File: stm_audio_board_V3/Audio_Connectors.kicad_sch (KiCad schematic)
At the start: 8 parts, among them J12 AudioJack_Loop2_Send, J13 AudioJack_Loop1_Send, J14 AudioJack_OUTPUT_Main, J15 AudioJack_Loop3_Return, J16 AudioJack_Loop2_Return, J7 AudioJack_Loop3_Send, J8 AudioJack_Loop1_Return, J9 AudioJack_INPUT_Main

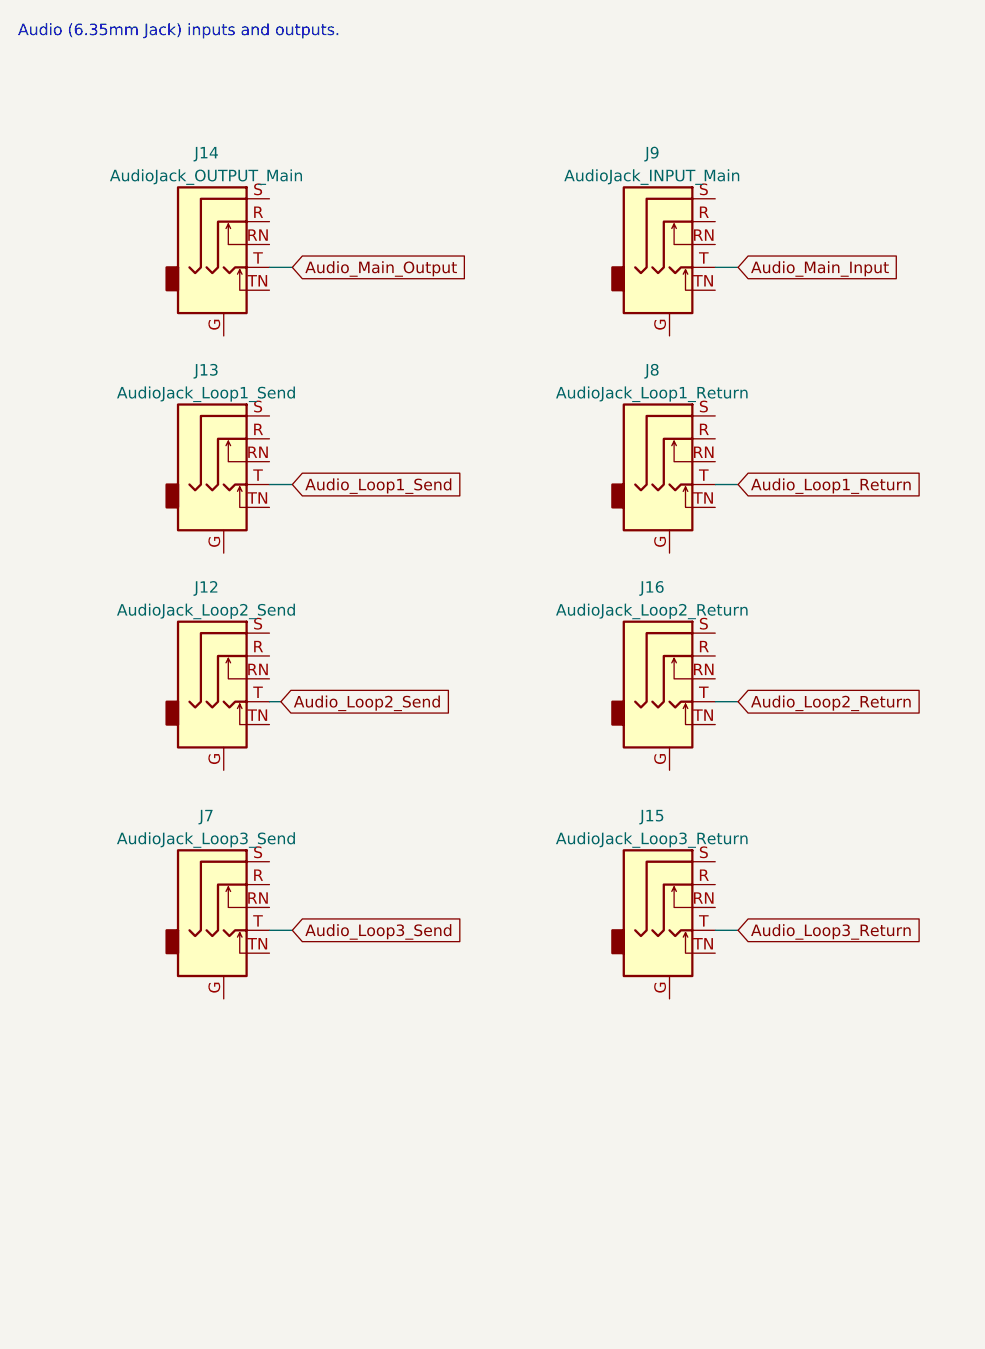
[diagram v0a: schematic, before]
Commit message: Reworked outline for enclosure
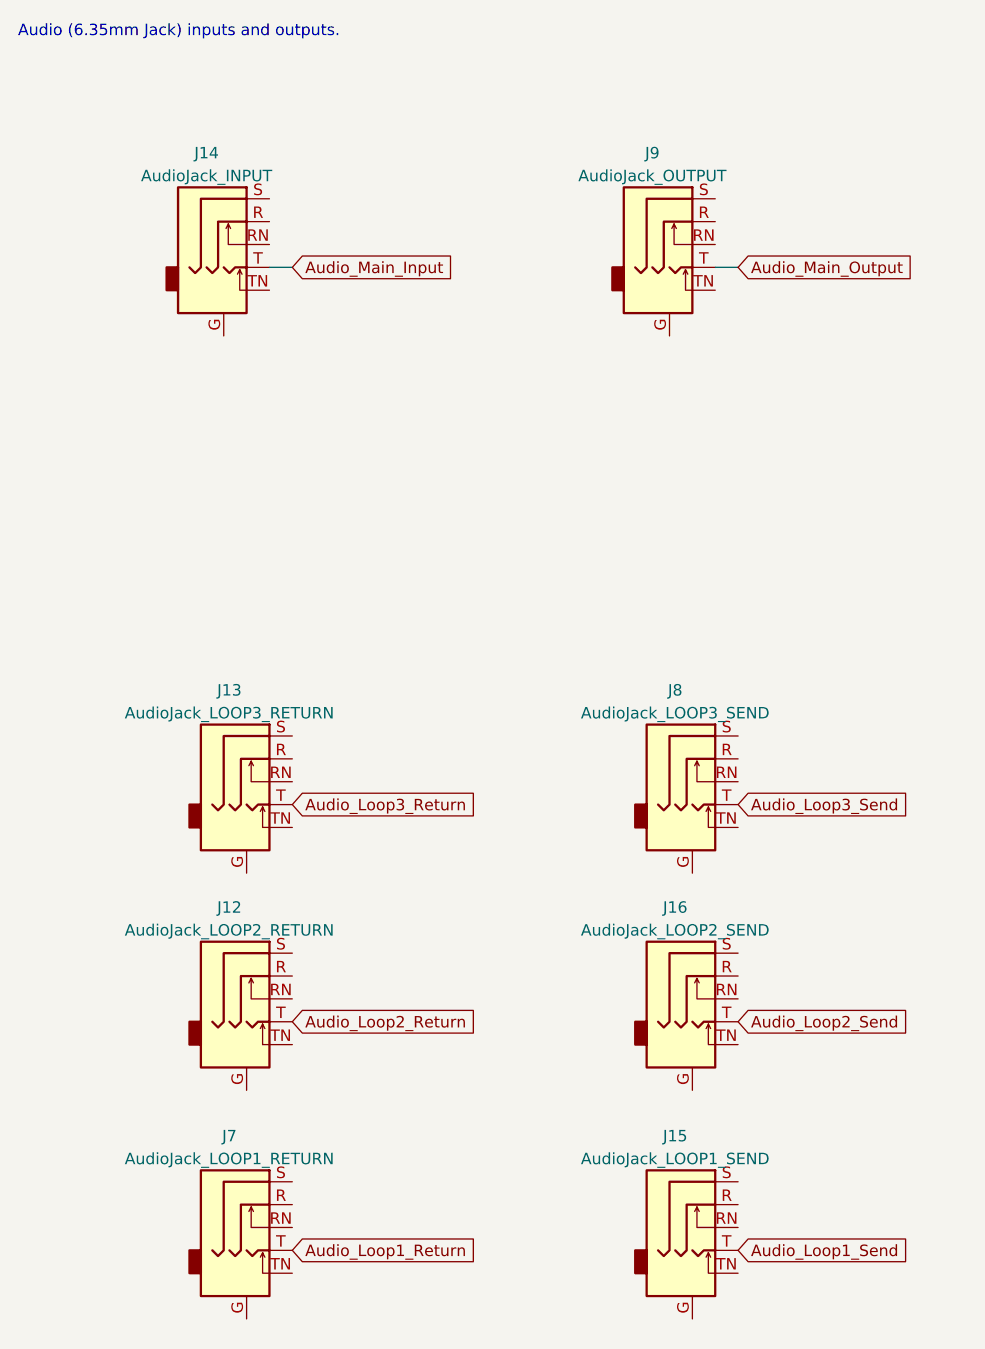
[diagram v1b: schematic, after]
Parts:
- J12: value AudioJack_Loop2_Send -> AudioJack_LOOP2_RETURN
- J13: value AudioJack_Loop1_Send -> AudioJack_LOOP3_RETURN
- J14: value AudioJack_OUTPUT_Main -> AudioJack_INPUT
- J15: value AudioJack_Loop3_Return -> AudioJack_LOOP1_SEND
- J16: value AudioJack_Loop2_Return -> AudioJack_LOOP2_SEND
- J7: value AudioJack_Loop3_Send -> AudioJack_LOOP1_RETURN
- J8: value AudioJack_Loop1_Return -> AudioJack_LOOP3_SEND
- J9: value AudioJack_INPUT_Main -> AudioJack_OUTPUT
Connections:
- net Audio_Loop1_Return: now also J7.T; no longer J8.T
- net Audio_Loop1_Send: now also J15.T; no longer J13.T
- net Audio_Loop2_Return: now also J12.T; no longer J16.T
- net Audio_Loop2_Send: now also J16.T; no longer J12.T
- net Audio_Loop3_Return: now also J13.T; no longer J15.T
- net Audio_Loop3_Send: now also J8.T; no longer J7.T
- net Audio_Main_Input: now also J14.T; no longer J9.T
- net Audio_Main_Output: now also J9.T; no longer J14.T
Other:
- moved on the sheet: J12, J13, J15, J16, J7, J8

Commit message: PCB design is finished
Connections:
- net GND: now reaches J14.TN
- net GND: now also J12.TN, J13.TN, J7.TN
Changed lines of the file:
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@@
+    )
+  )
+  (symbol (lib_id "power:GND") (at 45.72 45.72 0) (unit 1)
+    (in_bom yes) (on_board yes) (dnp no) (fields_autoplaced)
+    (property "Reference" "#PWR02" (at 45.72 52.07 0)
+      (effects (font (size 1.27 1.27)) hide)
+    )
+    (property "Value" "GND" (at 45.72 50.8 0)
+      (effects (font (size 1.27 1.27)))
+    )
+    (property "Footprint" "" (at 45.72 45.72 0)
+      (effects (font (size 1.27 1.27)) hide)
+    )
+    (property "Datasheet" "" (at 45.72 45.72 0)
+      (effects (font (size 1.27 1.27)) hide)
+    )
+    (pin "1")
+    (instances
+      (project "stm_audio_board_V3"
+        (path "/6997cf63-2615-4e49-9471-e7da1b6bae71"
+          (reference "#PWR02") (unit 1)
+        )
+        (path "/6997cf63-2615-4e49-9471-e7da1b6bae71/2eb2ee8f-ab98-4666-97f0-bfacb073bc88"
+          (reference "#PWR01") (unit 1)
+        )
+        (path "/6997cf63-2615-4e49-9471-e7da1b6bae71/f20dc640-ad21-4977-8df1-611625087c69"
+          (reference "#PWR013") (unit 1)
+        )
+        (path "/6997cf63-2615-4e49-9471-e7da1b6bae71/bf8ef258-4ec0-4b8f-b717-0a82eb791e29"
+          (reference "#PWR0249") (unit 1)
+        )
+      )
+    )
+  )
+  (symbol (lib_id "power:GND") (at 48.26 154.94 0) (unit 1)
+    (in_bom yes) (on_board yes) (dnp no) (fields_autoplaced)
+    (property "Reference" "#PWR02" (at 48.26 161.29 0)
+      (effects (font (size 1.27 1.27)) hide)
+    )
+    (property "Value" "GND" (at 48.26 160.02 0)
+      (effects (font (size 1.27 1.27)))
+    )
+    (property "Footprint" "" (at 48.26 154.94 0)
+      (effects (font (size 1.27 1.27)) hide)
+    )
+    (property "Datasheet" "" (at 48.26 154.94 0)
+      (effects (font (size 1.27 1.27)) hide)
+    )
+    (pin "1")
+    (instances
+      (project "stm_audio_board_V3"
+        (path "/6997cf63-2615-4e49-9471-e7da1b6bae71"
+          (reference "#PWR02") (unit 1)
+        )
+        (path "/6997cf63-2615-4e49-9471-e7da1b6bae71/2eb2ee8f-ab98-4666-97f0-bfacb073bc88"
+          (reference "#PWR01") (unit 1)
+        )
+        (path "/6997cf63-2615-4e49-9471-e7da1b6bae71/f20dc640-ad21-4977-8df1-611625087c69"
+          (reference "#PWR013") (unit 1)
+        )
+        (path "/6997cf63-2615-4e49-9471-e7da1b6bae71/bf8ef258-4ec0-4b8f-b717-0a82eb791e29"
+          (reference "#PWR0254") (unit 1)
+        )
+      )
     )
   )
@@
     )
   )
+  (symbol (lib_id "power:GND") (at 48.26 105.41 0) (unit 1)
+    (in_bom yes) (on_board yes) (dnp no) (fields_autoplaced)
+    (property "Reference" "#PWR02" (at 48.26 111.76 0)
+      (effects (font (size 1.27 1.27)) hide)
+    )
+    (property "Value" "GND" (at 48.26 110.49 0)
+      (effects (font (size 1.27 1.27)))
+    )
+    (property "Footprint" "" (at 48.26 105.41 0)
+      (effects (font (size 1.27 1.27)) hide)
+    )
+    (property "Datasheet" "" (at 48.26 105.41 0)
+      (effects (font (size 1.27 1.27)) hide)
+    )
+    (pin "1")
+    (instances
+      (project "stm_audio_board_V3"
+        (path "/6997cf63-2615-4e49-9471-e7da1b6bae71"
+          (reference "#PWR02") (unit 1)
+        )
+        (path "/6997cf63-2615-4e49-9471-e7da1b6bae71/2eb2ee8f-ab98-4666-97f0-bfacb073bc88"
+          (reference "#PWR01") (unit 1)
+        )
+        (path "/6997cf63-2615-4e49-9471-e7da1b6bae71/f20dc640-ad21-4977-8df1-611625087c69"
+          (reference "#PWR013") (unit 1)
+        )
+        (path "/6997cf63-2615-4e49-9471-e7da1b6bae71/bf8ef258-4ec0-4b8f-b717-0a82eb791e29"
+          (reference "#PWR0252") (unit 1)
+        )
+      )
+    )
+  )
   (symbol (lib_id "Connector_Audio:AudioJack3_Ground_SwitchTR") (at 90.17 38.1 0) (unit 1)
     (in_bom yes) (on_board yes) (dnp no) (fields_autoplaced)
@@
         )
       )
+    )
+  )
+  (symbol (lib_id "power:GND") (at 48.26 129.54 0) (unit 1)
+    (in_bom yes) (on_board yes) (dnp no) (fields_autoplaced)
+    (property "Reference" "#PWR02" (at 48.26 135.89 0)
+      (effects (font (size 1.27 1.27)) hide)
+    )
+    (property "Value" "GND" (at 48.26 134.62 0)
+      (effects (font (size 1.27 1.27)))
+    )
+    (property "Footprint" "" (at 48.26 129.54 0)
+      (effects (font (size 1.27 1.27)) hide)
+    )
+    (property "Datasheet" "" (at 48.26 129.54 0)
+      (effects (font (size 1.27 1.27)) hide)
+    )
+    (pin "1")
+    (instances
+      (project "stm_audio_board_V3"
+        (path "/6997cf63-2615-4e49-9471-e7da1b6bae71"
+          (reference "#PWR02") (unit 1)
+        )
+        (path "/6997cf63-2615-4e49-9471-e7da1b6bae71/2eb2ee8f-ab98-4666-97f0-bfacb073bc88"
+          (reference "#PWR01") (unit 1)
+        )
+        (path "/6997cf63-2615-4e49-9471-e7da1b6bae71/f20dc640-ad21-4977-8df1-611625087c69"
+          (reference "#PWR013") (unit 1)
+        )
+        (path "/6997cf63-2615-4e49-9471-e7da1b6bae71/bf8ef258-4ec0-4b8f-b717-0a82eb791e29"
+          (reference "#PWR0253") (unit 1)
+        )
+      )

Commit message: minor changes to components
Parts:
- J12, J13, J14, J15, J16, J7, J8, J9: LCSC Part (none) -> C309275
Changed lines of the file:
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@@
+      (effects (font (size 1.27 1.27)) hide)
+    )
+    (property "LCSC Part" "C309275" (at 92.71 147.32 0)
       (effects (font (size 1.27 1.27)) hide)
     )
@@
       (effects (font (size 1.27 1.27)) hide)
     )
+    (property "LCSC Part" "C309275" (at 92.71 97.79 0)
+      (effects (font (size 1.27 1.27)) hide)
+    )
     (pin "G")
     (pin "R")
@@
     )
     (property "Datasheet" "~" (at 40.64 38.1 0)
+      (effects (font (size 1.27 1.27)) hide)
+    )
+    (property "LCSC Part" "C309275" (at 40.64 38.1 0)
       (effects (font (size 1.27 1.27)) hide)
     )
@@
       (effects (font (size 1.27 1.27)) hide)
     )
+    (property "LCSC Part" "C309275" (at 43.18 121.92 0)
+      (effects (font (size 1.27 1.27)) hide)
+    )
     (pin "G")
     (pin "R")
@@
       (effects (font (size 1.27 1.27)) hide)
     )
+    (property "LCSC Part" "C309275" (at 90.17 38.1 0)
+      (effects (font (size 1.27 1.27)) hide)
+    )
     (pin "G")
     (pin "R")
@@
       (effects (font (size 1.27 1.27)) hide)
     )
+    (property "LCSC Part" "C309275" (at 92.71 121.92 0)
+      (effects (font (size 1.27 1.27)) hide)
+    )
     (pin "G")
     (pin "R")
@@
       (effects (font (size 1.27 1.27)) hide)
     )
+    (property "LCSC Part" "C309275" (at 43.18 97.79 0)
+      (effects (font (size 1.27 1.27)) hide)
+    )
     (pin "G")
     (pin "R")
@@
       (effects (font (size 1.27 1.27)) hide)
     )
+    (property "LCSC Part" "C309275" (at 43.18 147.32 0)
+      (effects (font (size 1.27 1.27)) hide)
+    )
